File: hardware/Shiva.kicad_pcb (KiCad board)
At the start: 2 copper layers, 99.8 x 99.8 mm, 77 parts, among them J1 JACK_FEMALE_STEREO, J2 JACK_FEMALE_STEREO, J3 JACK_FEMALE_STEREO, J4 JACK_FEMALE_STEREO, J5 JACK_FEMALE_STEREO, J6 JACK_FEMALE_STEREO, J7 JACK_FEMALE_STEREO, J8 JACK_FEMALE_STEREO, P1 DIN_5, U1 LTC6242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

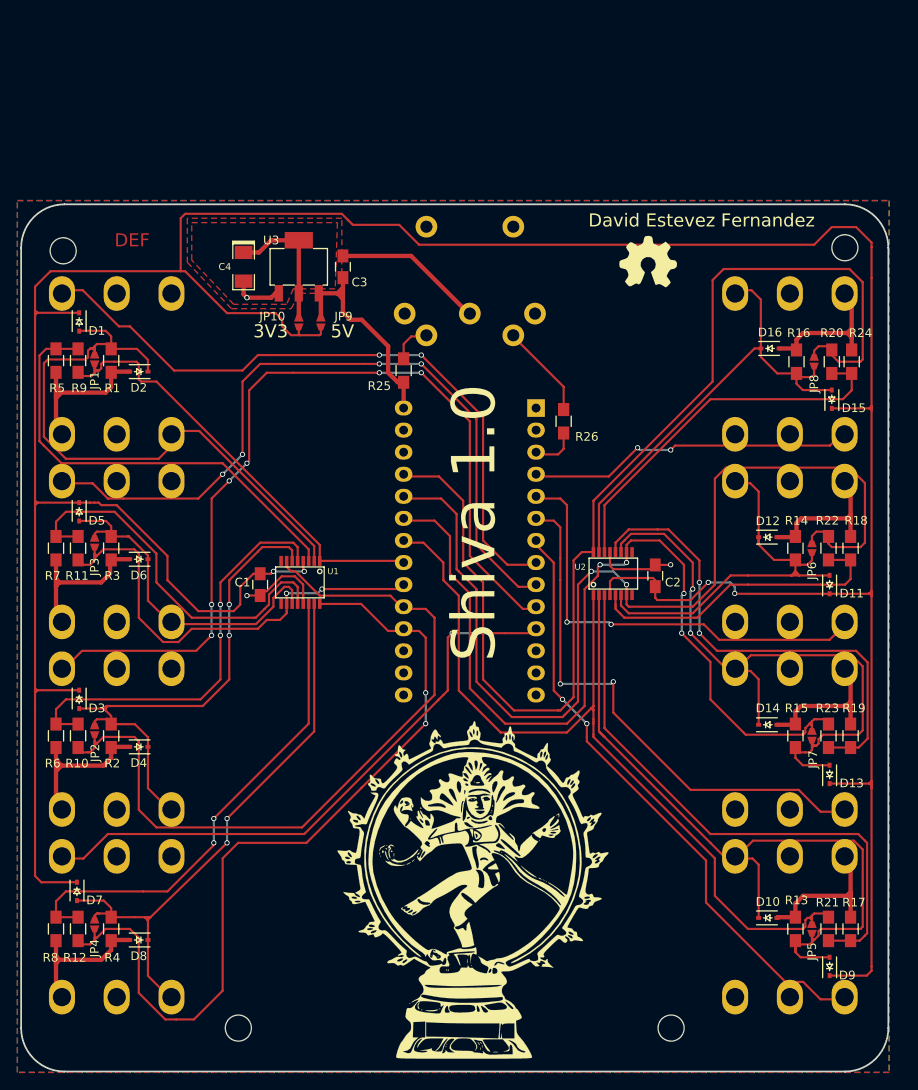
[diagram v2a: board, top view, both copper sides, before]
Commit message: Fix SMD footprints too small
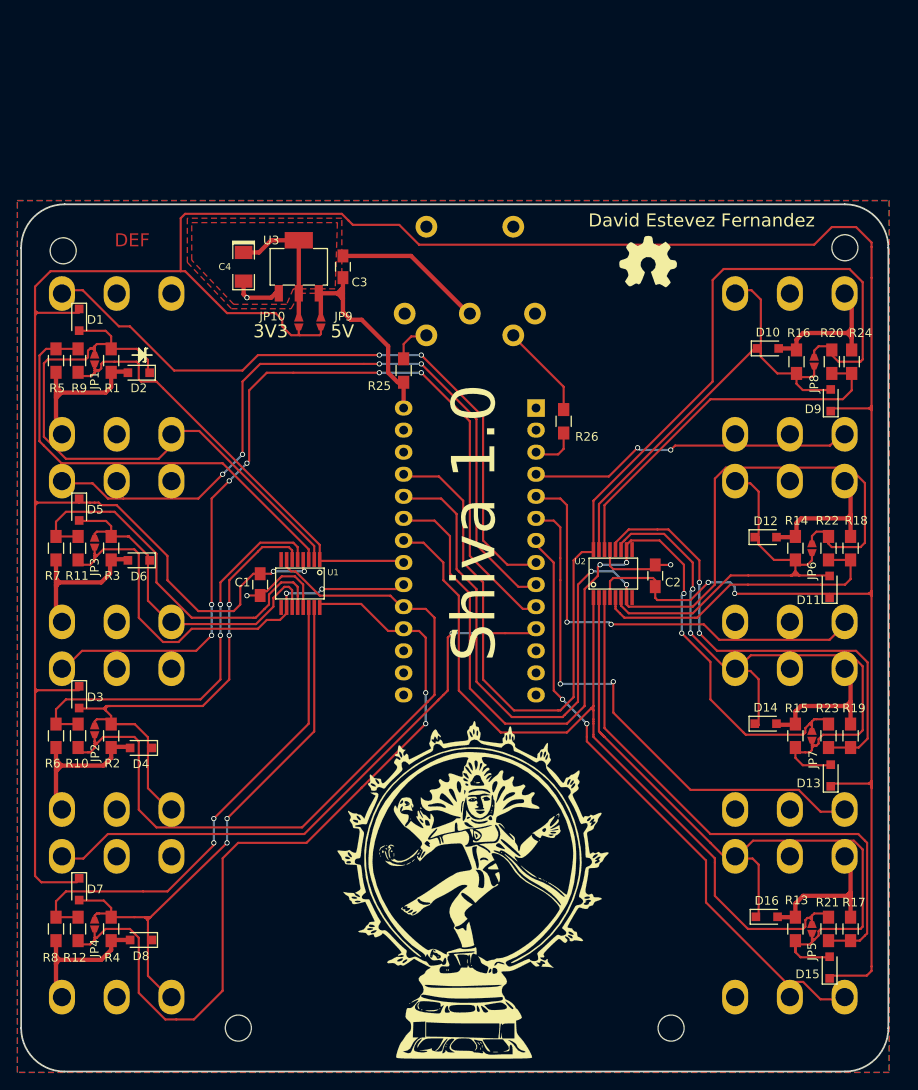
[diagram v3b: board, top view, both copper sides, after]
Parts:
- D1, D10, D11, D12, D13, D14, D15, D16, D2, D3, D4, D5, D6, D7, D8, D9: footprint Diodes_SMD:SOD-323 -> Diodes_SMD:D_SOD-323_HandSoldering
- moved D10 65.5 mm to (180.3, 69.3)
- moved D16 65.4 mm to (180.2, 134.7)
- moved D15 65.4 mm to (187.5, 140.6)
- moved D9 65.2 mm to (187.6, 75.3)
- moved D7 0.36 mm to (101.1, 131.6)
- moved D4 0.28 mm to (108.2, 115.3)
- moved D14 0.28 mm to (180.1, 112.5)
- moved D11 0.25 mm to (187.5, 96.8)
- moved D5 0.25 mm to (101.1, 87.9)
- moved D1 0.25 mm to (101.1, 66.0)
- moved D12 0.25 mm to (180.1, 91.1)
- moved D3 0.25 mm to (101.1, 109.5)
- moved D8 0.25 mm to (108.2, 137.4)
- moved D13 0.18 mm to (187.6, 118.5)
- moved D2 0.13 mm to (108.0, 72.1)
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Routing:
- net Net-(D10-Pad1): track 108.4 -> 140.1 mm
- net Net-(D15-Pad2): track 88.9 -> 57.2 mm
- net Net-(J1-PadTS): track 30.3 -> 21.3 mm
- net Net-(D1-Pad2): track 70.7 -> 79.8 mm
- net GND: track 553.0 -> 557.6 mm
- net /DETECT_07: track 41.0 -> 36.4 mm
- net Net-(R19-Pad1): track 4.43 -> 4.97 mm
- net Net-(J7-PadTS): track 29.6 -> 29.0 mm

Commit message: Change placement of required components
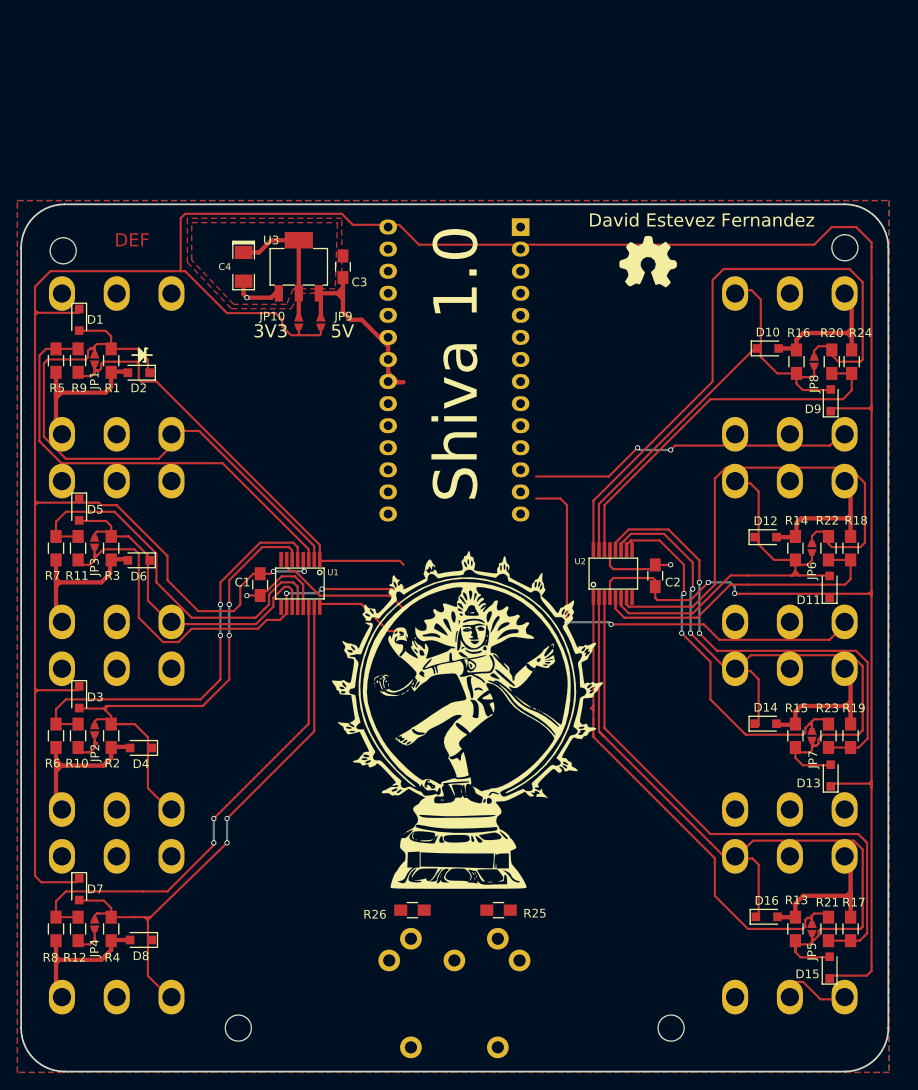
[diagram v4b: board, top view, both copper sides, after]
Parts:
- moved P1 99.5 mm to (144.3, 152.3), turned to 180 degrees
- moved R25 63.1 mm to (149.4, 134.0), turned to 0 degrees
- moved R26 58.9 mm to (139.4, 134.0), turned to 180 degrees
- moved G*** 22.1 mm to (144.4, 106.2)
- moved G*** 22.0 mm to (144.3, 124.3)
- moved BOARD1 20.9 mm to (144.3, 73.2)
- moved G*** 19.6 mm to (145.7, 112.0)
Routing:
- net GND: track 557.6 -> 239.8 mm, vias 17 -> 7
- net /CHANNEL_01: track 96.9 -> 14.6 mm, vias 2 -> 0
- net /DETECT_03: track 73.9 -> 4.57 mm, vias 4 -> 0
- net /CHANNEL_02: track 89.3 -> 22.1 mm
- net /CHANNEL_06: track 91.4 -> 28.7 mm, vias 2 -> 0
- net /CHANNEL_07: track 106.2 -> 44.5 mm, vias 4 -> 2
- net /CHANNEL_05: track 132.6 -> 72.1 mm
- net /CHANNEL_08: track 98.2 -> 58.8 mm
- net Net-(J8-PadR): track 38.9 -> 1.78 mm
- net /DETECT_08: track 30.0 -> 4.75 mm, vias 2 -> 0
- net Net-(P1-Pad4): track 10.8 -> 0.00 mm
- net /DETECT_01: track 15.2 -> 5.47 mm, vias 2 -> 0
- net /DETECT_05: track 13.9 -> 5.47 mm
- net Net-(R18-Pad1): track 18.0 -> 9.64 mm
- net Net-(D11-Pad2): track 65.2 -> 73.6 mm
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
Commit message: Reroute channel 4
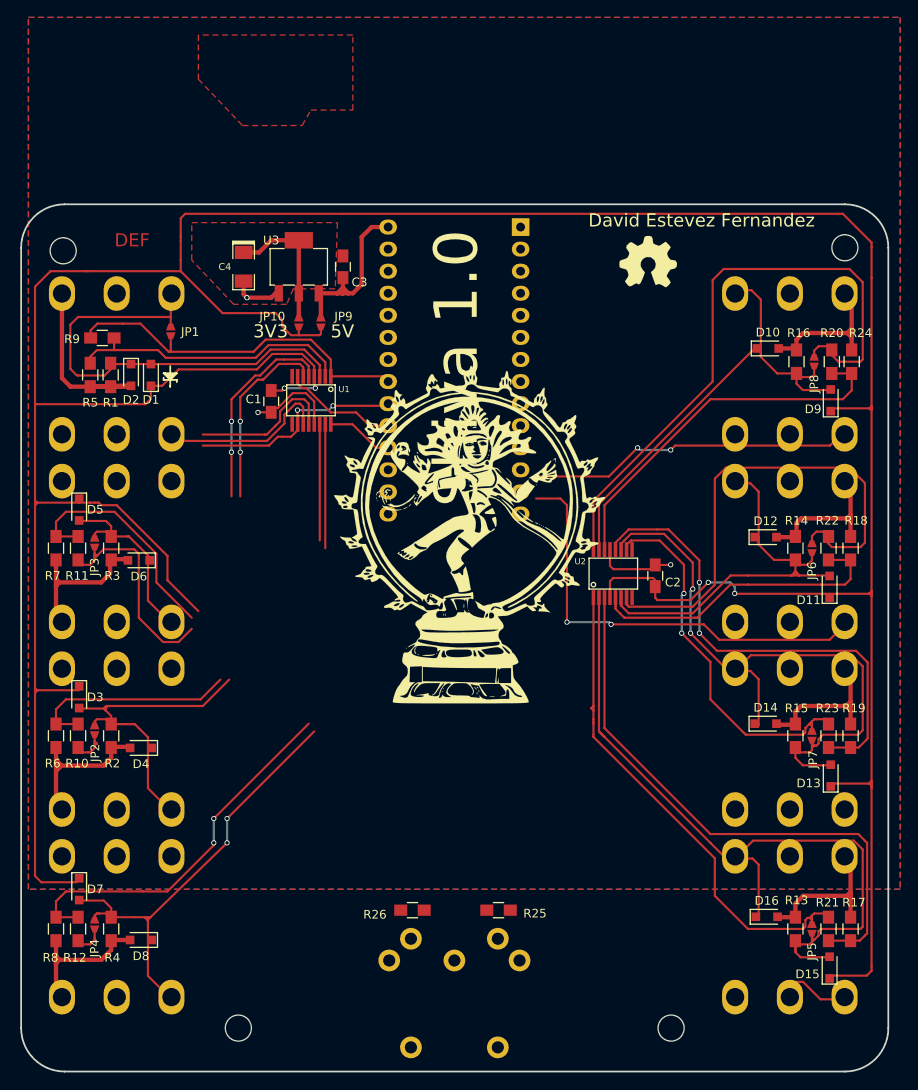
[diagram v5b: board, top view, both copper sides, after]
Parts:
- moved G*** 21.3 mm to (145.9, 90.7)
- moved C1 21.1 mm to (123.2, 75.4)
- moved G*** 21.1 mm to (145.7, 85.1)
- moved U1 21.1 mm to (127.5, 75.3)
- moved D1 10.4 mm to (109.3, 72.4), turned to 90 degrees
- moved JP1 9.34 mm to (111.6, 67.4)
- moved R5 4.27 mm to (102.4, 72.4)
- moved R9 3.82 mm to (103.8, 68.1), turned to 0 degrees
- moved R1 1.65 mm to (104.7, 72.4)
- moved D2 0.92 mm to (107.1, 72.4), turned to 270 degrees
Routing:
- net Net-(R12-Pad2): track 19.0 -> 58.4 mm, vias 0 -> 2
- net Net-(D7-Pad2): track 103.3 -> 64.0 mm, vias 4 -> 2
- net Net-(D1-Pad2): track 79.8 -> 54.0 mm
- net VCC: track 393.5 -> 413.0 mm
- net Net-(D3-Pad2): track 79.0 -> 62.7 mm
- net Net-(R10-Pad2): track 30.2 -> 46.2 mm
- net +5V: track 35.9 -> 21.4 mm
- net Net-(J1-PadTS): track 21.3 -> 9.73 mm
- net Net-(J3-PadTS): track 13.6 -> 3.83 mm
- net GND: track 239.8 -> 249.2 mm
- net /CHANNEL_04: track 52.3 -> 43.0 mm
- net Net-(R5-Pad1): track 24.1 -> 33.4 mm
- net /DETECT_04: track 6.56 -> 3.09 mm
- net /CHANNEL_01: track 14.6 -> 11.3 mm
- net /CHANNEL_02: track 22.1 -> 19.0 mm
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
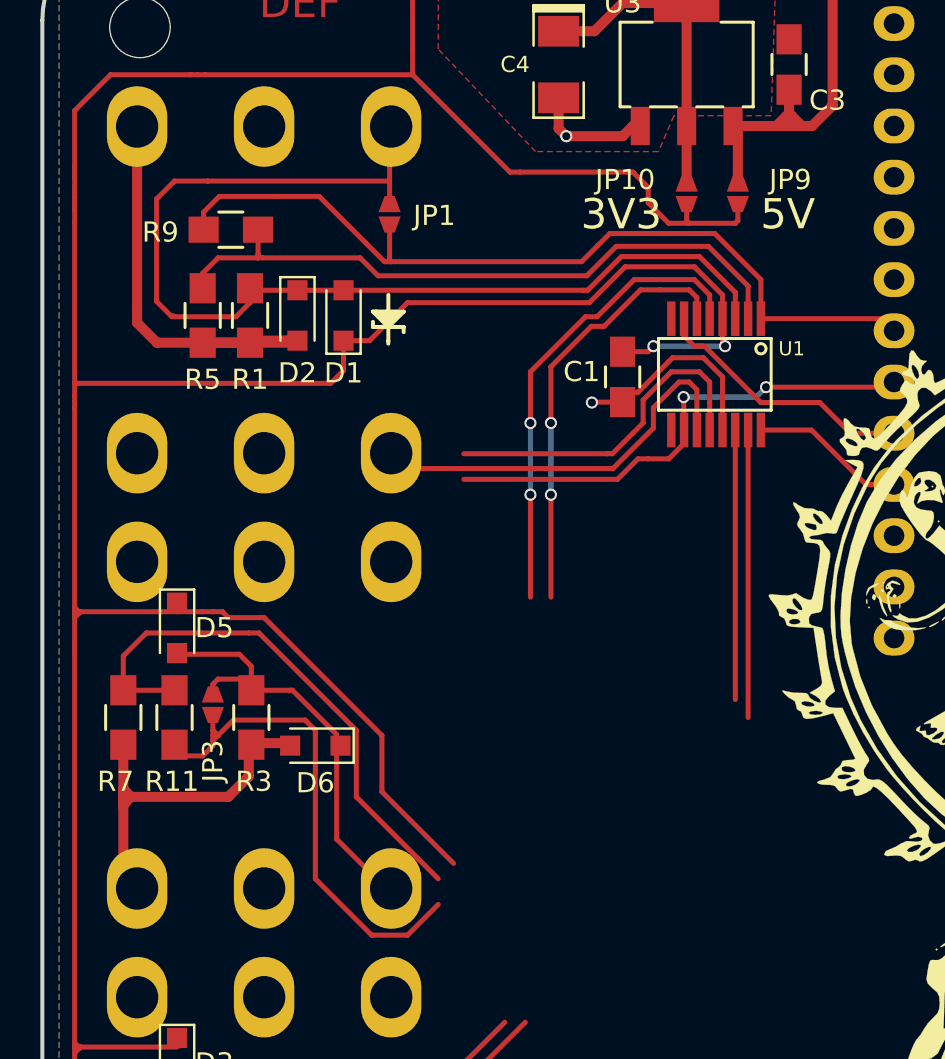
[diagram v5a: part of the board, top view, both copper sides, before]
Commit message: Route channel 3
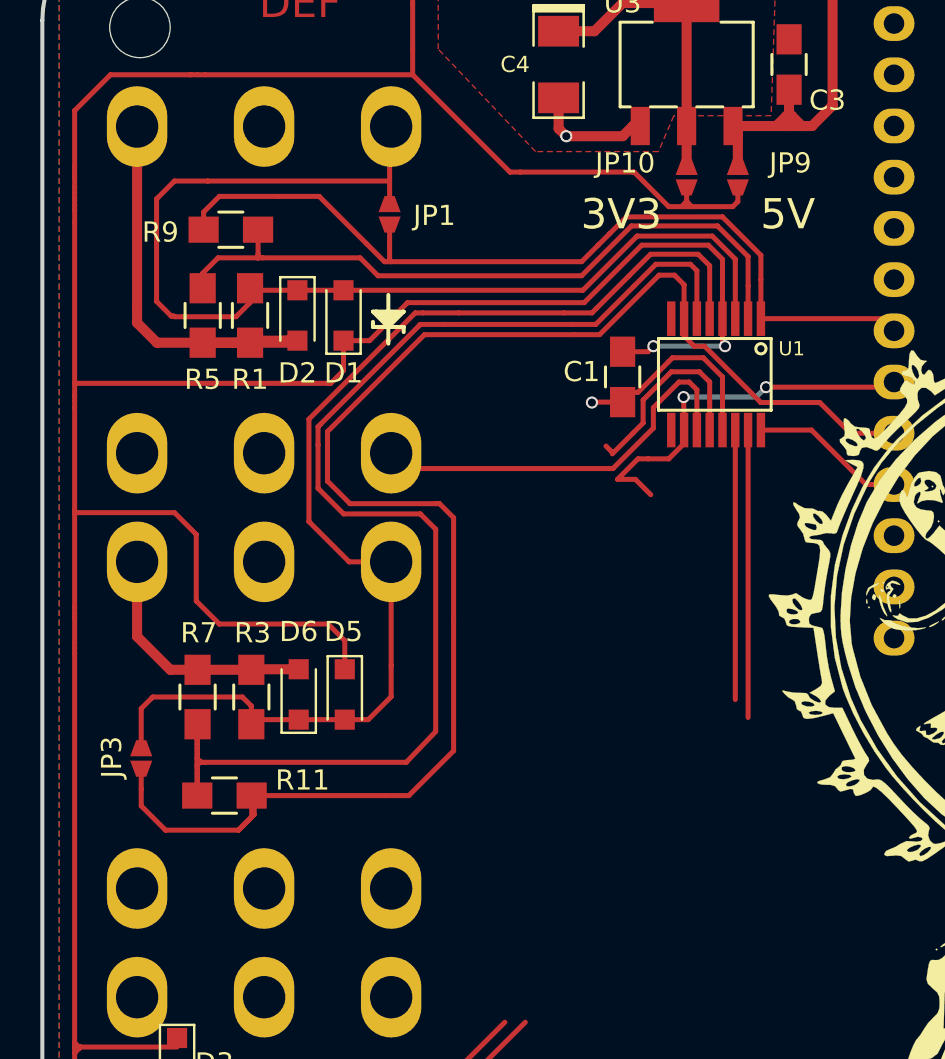
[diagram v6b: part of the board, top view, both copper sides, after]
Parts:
- moved D5 8.95 mm to (109.4, 91.2)
- moved R11 4.60 mm to (103.4, 96.2), turned to 180 degrees
- moved JP3 4.45 mm to (99.3, 94.4)
- moved R7 3.82 mm to (102.1, 91.3), turned to 90 degrees
- moved D6 2.67 mm to (107.1, 91.2), turned to 90 degrees
- moved R3 1.02 mm to (104.8, 91.3), turned to 90 degrees
- moved JP10 0.83 mm to (126.4, 65.5)
- moved JP9 0.83 mm to (128.9, 65.5)
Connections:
- BOARD1 pad 19: /CHANNEL_02 -> /CHANNEL_03
- BOARD1 pad 20: /CHANNEL_03 -> /CHANNEL_02
- U1 pad 10: /CHANNEL_03 -> /CHANNEL_02
- U1 pad 11: Net-(R11-Pad2) -> Net-(R10-Pad2)
- U1 pad 12: Net-(D5-Pad2) -> Net-(D3-Pad2)
- U1 pad 5: Net-(D3-Pad2) -> Net-(D5-Pad2)
- U1 pad 6: Net-(R10-Pad2) -> Net-(R11-Pad2)
- U1 pad 7: /CHANNEL_02 -> /CHANNEL_03
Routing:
- net Net-(R11-Pad2): track 35.6 -> 65.2 mm
- net /CHANNEL_03: track 50.2 -> 79.5 mm, vias 2 -> 0
- net Net-(D5-Pad2): track 35.8 -> 59.5 mm
- net Net-(D3-Pad2): track 62.7 -> 49.1 mm, vias 2 -> 0
- net Net-(R10-Pad2): track 46.2 -> 32.9 mm, vias 2 -> 0
- net /CHANNEL_02: track 19.0 -> 25.0 mm, vias 0 -> 2
- net VCC: track 413.0 -> 407.9 mm
- net Net-(J3-PadTS): track 3.83 -> 0.00 mm
- net /DETECT_03: track 4.57 -> 0.97 mm
- net GND: track 249.2 -> 246.1 mm
- net Net-(D1-Pad2): track 54.0 -> 55.8 mm
- net Net-(R5-Pad1): track 33.4 -> 35.1 mm
- net /CHANNEL_04: track 43.0 -> 44.4 mm
- net Net-(C4-Pad1): track 16.9 -> 16.1 mm
- net +5V: track 21.4 -> 20.6 mm

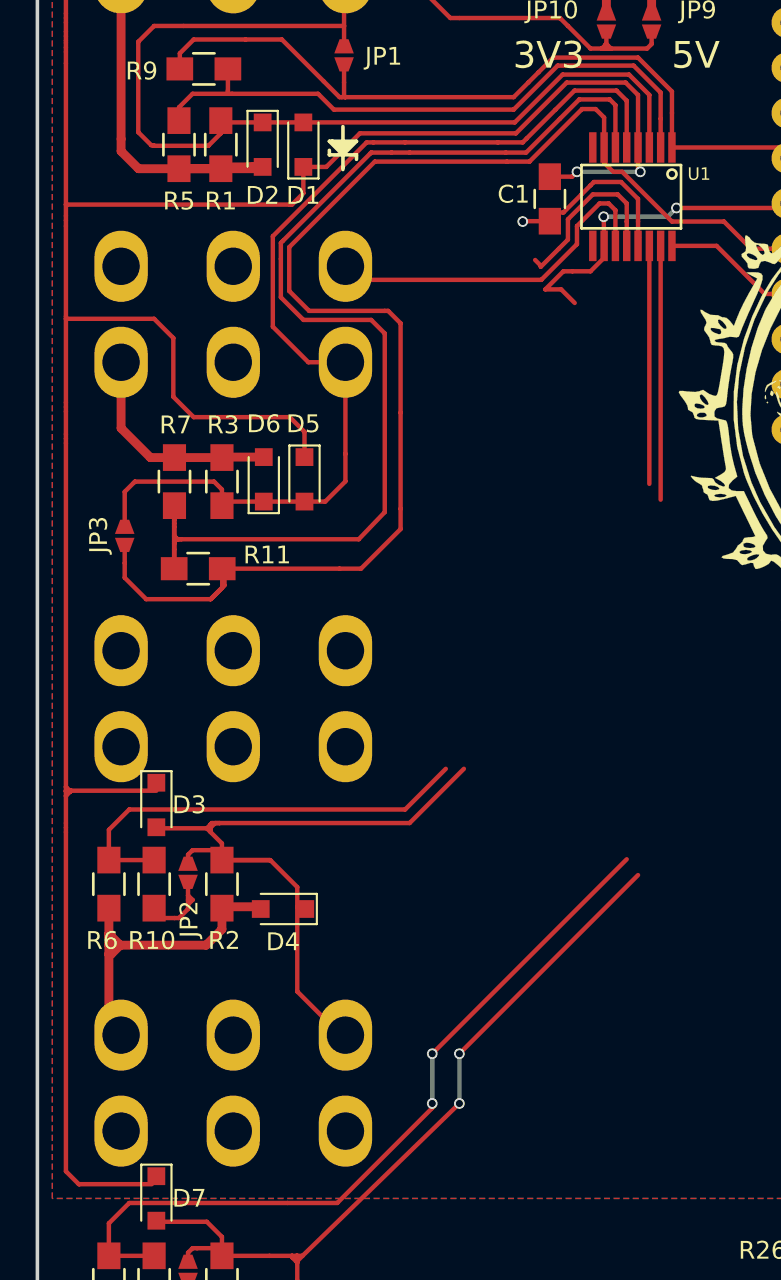
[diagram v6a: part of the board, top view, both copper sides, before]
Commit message: Route channel 2
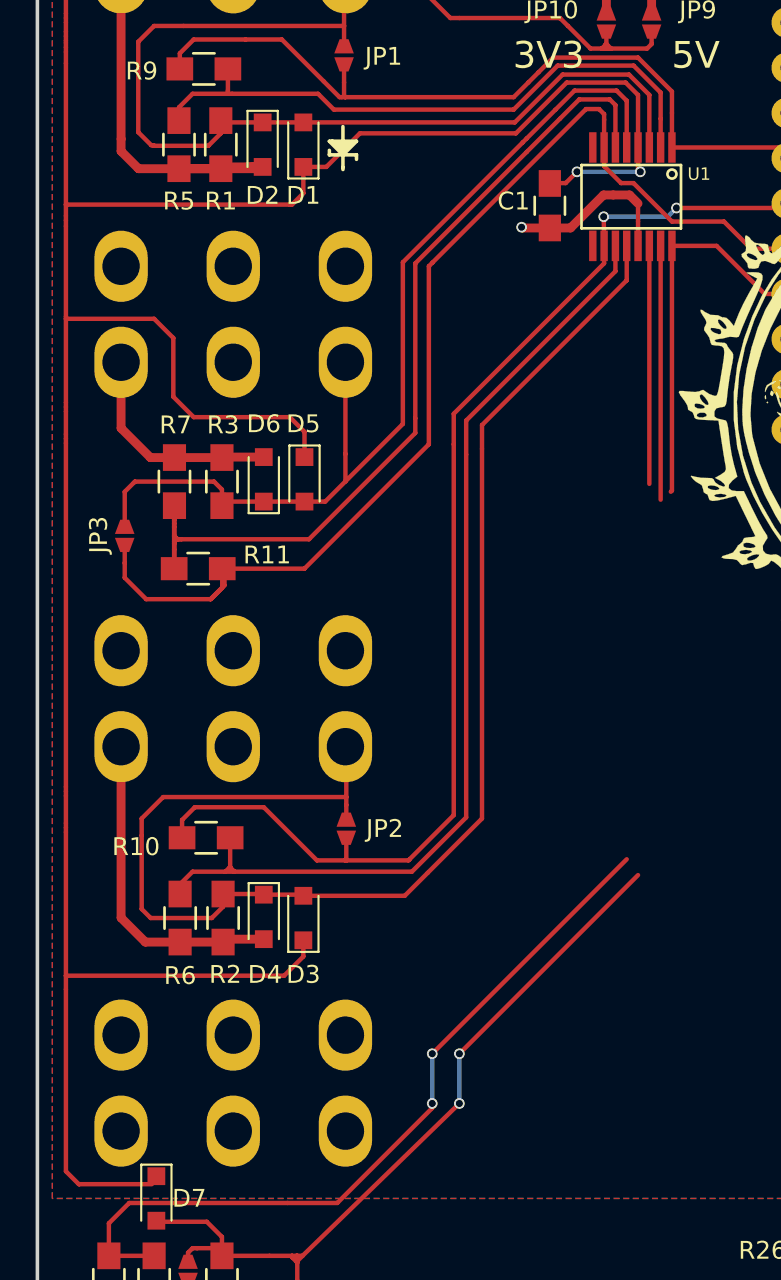
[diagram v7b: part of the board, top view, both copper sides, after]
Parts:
- moved D3 10.4 mm to (109.3, 115.8), turned to 90 degrees
- moved JP2 9.23 mm to (111.8, 110.8)
- moved R6 4.43 mm to (102.4, 115.8)
- moved R10 3.91 mm to (103.9, 111.3), turned to 0 degrees
- moved R2 1.91 mm to (104.8, 115.8)
- moved D4 1.17 mm to (107.1, 115.8), turned to 270 degrees
- moved C1 0.38 mm to (123.2, 75.8)
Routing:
- net /CHANNEL_02: track 25.0 -> 68.7 mm
- net Net-(D3-Pad2): track 49.1 -> 78.9 mm
- net Net-(R10-Pad2): track 32.9 -> 56.1 mm
- net Net-(R11-Pad2): track 65.2 -> 51.3 mm
- net /CHANNEL_01: track 11.3 -> 25.2 mm
- net /CHANNEL_03: track 79.5 -> 65.8 mm
- net Net-(J1-PadTS): track 9.73 -> 0.00 mm
- net VCC: track 407.9 -> 416.8 mm
- net GND: track 246.1 -> 251.1 mm
- net /DETECT_02: track 6.23 -> 2.12 mm
- net Net-(J2-PadTS): track 3.83 -> 0.00 mm
- net Net-(D5-Pad2): track 59.5 -> 56.4 mm
